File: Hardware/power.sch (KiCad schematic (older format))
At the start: 82 parts, among them J2 USB_B_Micro, J3 B2B-XH-A, J4 POWER ON, Q2 FDC638P, Q3 IRLML6244TRPBF, Q4 BSS138, Q5 BSS138, Q6 IRLML6244TRPBF, Q7 FDC638P, U10 TPS63900DSKR, U11 SiP32431DR3, U12 SiP32431DR3, U8 TP4056, U9 USBLC6-2SC6

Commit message: Add pcb route and ground plane
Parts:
- removed C25: 1u, Capacitor_SMD:C_0603_1608Metric, symbol Device:C
- removed D3, D4, D5, D6: 1N4148, Diode_THT:D_DO-35_SOD27_P7.62mm_Horizontal, symbol Diode:1N4148
- removed DFE252012P-2R2M=P2__2.2µH1: 2.2uH, symbol Device:L
- removed J2: USB_B_Micro, Connector_USB:USB_Micro-B_Wuerth_614105150721_Vertical, symbol Connector:USB_B_Micro
- removed Q4, Q5: BSS138, Package_TO_SOT_SMD:SOT-23, symbol Transistor_FET:BSS138
- removed R58, R59: 0R, Resistor_SMD:R_0603_1608Metric, symbol Device:R
- removed TP19, TP22, TP23, TP24, TP25, TP27, TP29, TP30: TestPoint, TestPoint:TestPoint_Pad_D1.5mm, symbol Connector:TestPoint
- removed U11, U12: SiP32431DR3, Package_TO_SOT_SMD:SOT-363_SC-70-6, symbol Power_Management:SiP32431DR3
- removed U9: USBLC6-2SC6, Package_TO_SOT_SMD:SOT-23-6, symbol Power_Protection:USBLC6-2SC6
- added C44: 0.1u, Capacitor_SMD:C_0603_1608Metric, symbol Device:C
- added D3, D4, D5: 1N4148WT, EcoApi_pcb:SODFL1608X70N, symbol EcoApi_pcb:1N4148WT
- added D8: USBLC6-2SC6, EcoApi_pcb:SOT95P280X145-6N, symbol EcoApi_pcb:USBLC6-2SC6
- added IC2, IC3: SIP32431DR3-T1GE3, EcoApi_pcb:SOT65P210X110-6N, symbol EcoApi_pcb:SIP32431DR3-T1GE3
- added J2: 614105150721, EcoApi_pcb:WURTH_614105150721, symbol EcoApi_pcb:614105150721
- added L2: DFE252012P-2R2M=P2, EcoApi_pcb:INDC2520X120N, symbol EcoApi_pcb:DFE252012P-2R2M=P2
- added Q4, Q5: BSS138, EcoApi_pcb:SOT95P240X111-3N, symbol EcoApi_pcb:BSS138
- added R12, R13: 0R, Resistor_SMD:R_0603_1608Metric, symbol Device:R
- C28: value 0.1u -> 1u
- D1: value LED_0805 -> LED_0603_RED; footprint (none) -> LED_SMD:LED_0603_1608Metric
- D2: value LED_0805 -> LED_0603_GREEN; footprint (none) -> LED_SMD:LED_0603_1608Metric
- D6: renamed from D?; footprint SODFL1608X70N -> EcoApi_pcb:SODFL1608X70N
- TP20, TP21, TP26, TP28: footprint TestPoint:TestPoint_Pad_D1.5mm -> TestPoint:TestPoint_Pad_D1.0mm
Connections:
- wire segments 256 -> 253
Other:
- moved on the sheet: C16, C17, C19, C20, C21, C22, D1, D2, D6, F1, FB1, FB2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

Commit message: Fix drc error
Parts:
- F1, F2: footprint EcoApi_pcb:0603-F1608X100N -> EcoApi_pcb:FUSC1608X100N
- U10: footprint EcoApi_pcb:TPS63900DSKR -> EcoApi_pcb:SON50P250X250X80-11N-D
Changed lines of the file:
@@
 F 0 "U10" H 6000 2337 60  0000 C CNN
 F 1 "TPS63900DSKR" H 6000 2231 60  0000 C CNN
-F 2 "EcoApi_pcb:TPS63900DSKR" H 6000 1300 60  0001 C CNN
+F 2 "EcoApi_pcb:SON50P250X250X80-11N-D" H 6000 1300 60  0001 C CNN
 F 3 "" H 6000 1600 60  0001 C CNN
 	1    6000 1850
@@
 F 0 "F1" V 1165 5850 50  0000 C CNN
 F 1 "MF-FSMF050X-2" V 1256 5850 50  0000 C CNN
-F 2 "EcoApi_pcb:0603-F1608X100N" H 1400 5850 50  0001 L BNN
+F 2 "EcoApi_pcb:FUSC1608X100N" H 1400 5850 50  0001 L BNN
 F 3 "" H 1400 5850 50  0001 L BNN
 F 4 "MF-FSMF050X-2" H 1400 5850 50  0001 L BNN "MPN"
@@
 F 0 "F2" V 2465 1750 50  0000 C CNN
 F 1 "MF-FSMF050X-2" V 2556 1750 50  0000 C CNN
-F 2 "EcoApi_pcb:0603-F1608X100N" H 2700 1750 50  0001 L BNN
+F 2 "EcoApi_pcb:FUSC1608X100N" H 2700 1750 50  0001 L BNN
 F 3 "" H 2700 1750 50  0001 L BNN
 F 4 "MF-FSMF050X-2" H 2700 1750 50  0001 L BNN "MPN"

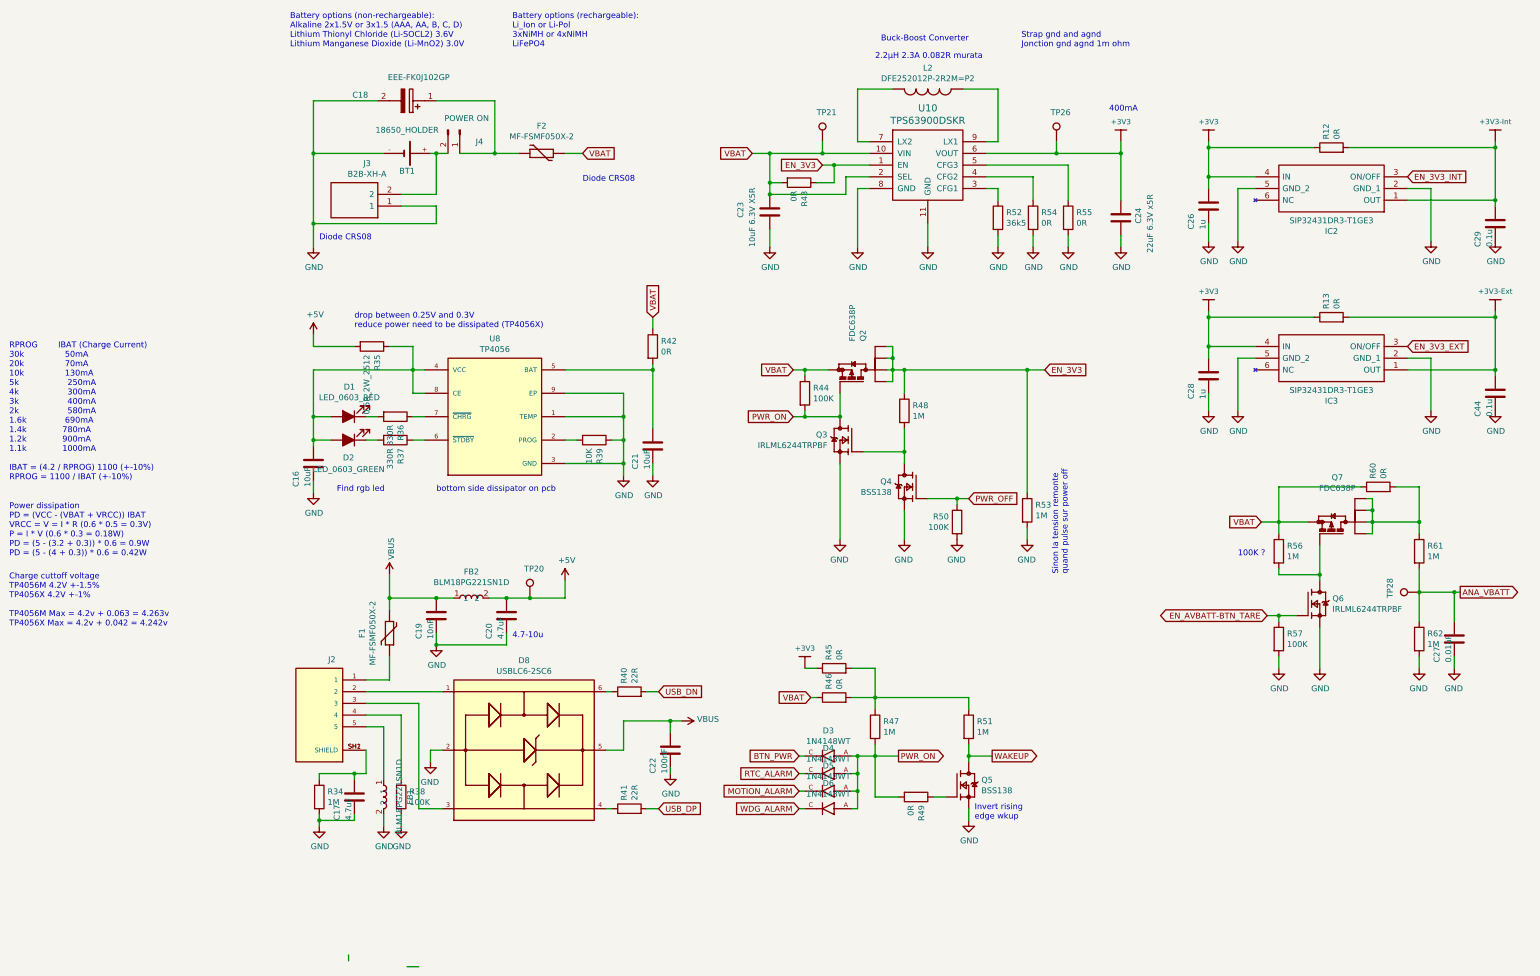
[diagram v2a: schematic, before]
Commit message: Update pcb to v2.1 (Add ldo)
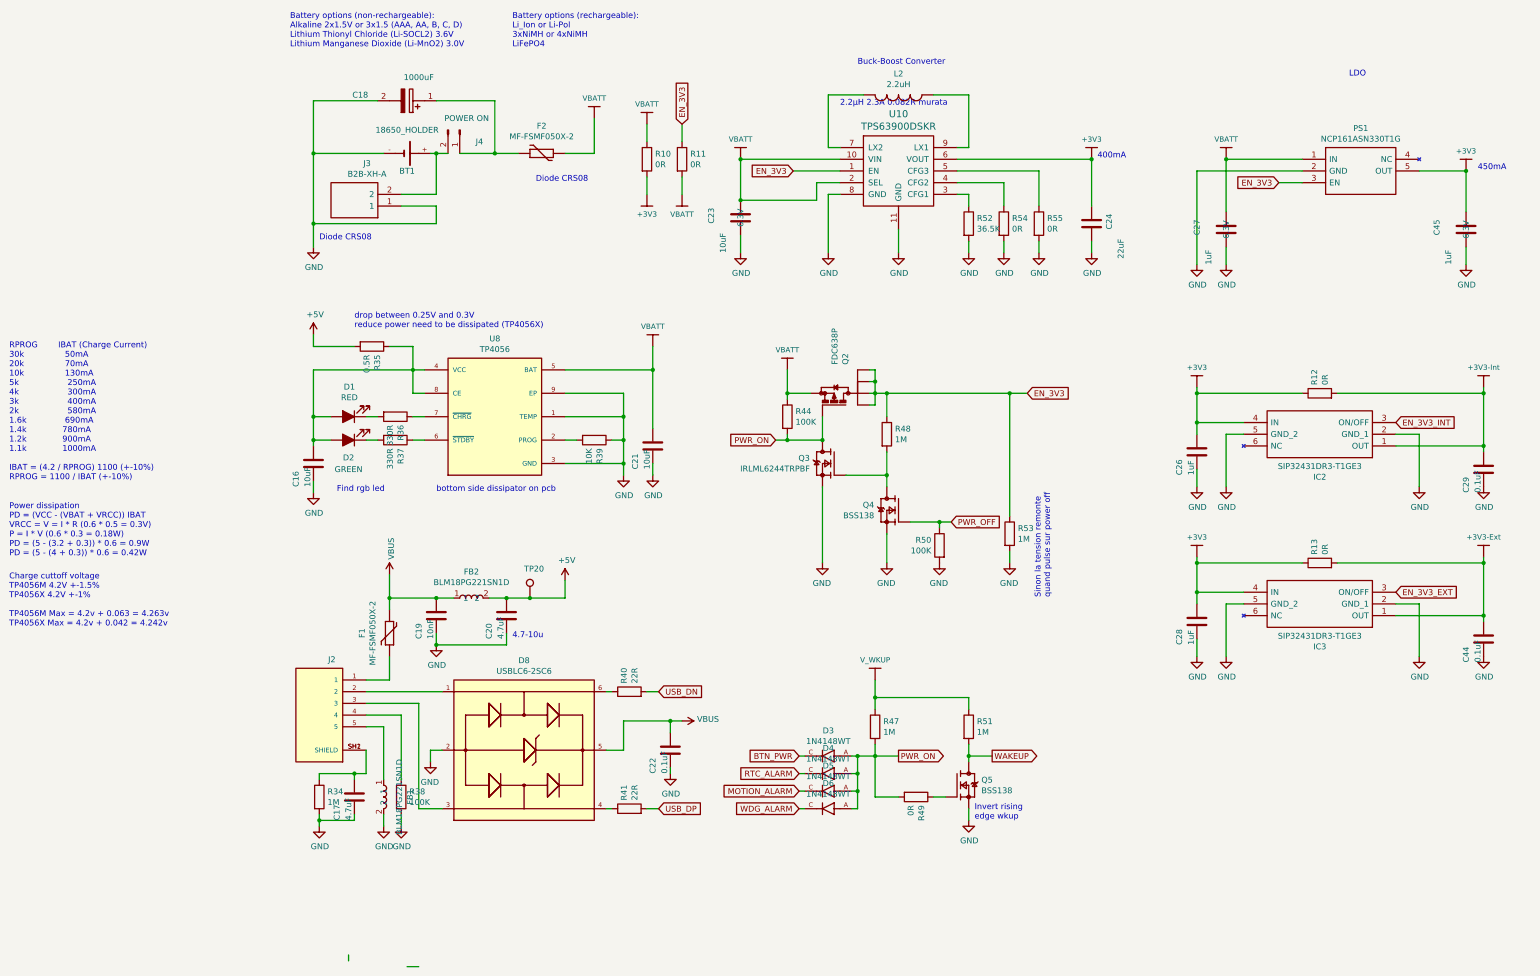
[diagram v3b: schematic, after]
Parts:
- removed Q6: IRLML6244TRPBF, EcoApi_pcb:SOT95P237X112-3N, symbol EcoApi_pcb:IRLML6244TRPBF
- removed Q7: FDC638P, EcoApi_pcb:SSOT-6, symbol EcoApi_pcb:FDC638P
- removed R42, R43, R45, R46, R60: 0R, Resistor_SMD:R_0603_1608Metric, symbol Device:R
- removed R56, R61, R62: 1M, Resistor_SMD:R_0603_1608Metric, symbol Device:R
- removed R57: 100K, Resistor_SMD:R_0603_1608Metric, symbol Device:R
- removed TP21, TP26, TP28: TestPoint, TestPoint:TestPoint_Pad_D1.0mm, symbol Connector:TestPoint
- added C45: 1uF, Capacitor_SMD:C_0603_1608Metric, symbol Device:C
- added PS1: NCP161ASN330T1G, EcoApi_pcb:SOT95P280X145-5N, symbol EcoApi_pcb:NCP161ASN330T1G
- added R10: 0R, Resistor_SMD:R_1206_3216Metric, symbol Device:R
- added R11: 0R, Resistor_SMD:R_0603_1608Metric, symbol Device:R
- BT1, J2, J3, J4: Populate (none) -> no
- C16, C17, C19, C20, C21, FB1, FB2: Populate (none) -> yes; Size Inch (none) -> 0603; Size Metric (none) -> 1608
- C18: value EEE-FK0J102GP -> 1000uF; Manufacturer_Name (none) -> Panasonic; Manufacturer_Part_Number (none) -> EEE-FK0J102GP; Populate (none) -> no; Tolerance (none) -> 20%; Voltage (none) -> 6.3V
- C22: value 100nF -> 0.1uF; Populate (none) -> yes; Size Inch (none) -> 0603; Size Metric (none) -> 1608
- C23: value 10uF 6.3V X5R -> 10uF; Dielectric (none) -> X5R; Populate (none) -> yes; Size Inch (none) -> 0603; Size Metric (none) -> 1608; Voltage (none) -> 6.3V
- C24: value 22uF 6.3V x5R -> 22uF; Dielectric (none) -> X5R; Populate (none) -> yes; Size Inch (none) -> 0603; Size Metric (none) -> 1608; Voltage (none) -> 6.3V
- C26, C28: value 1u -> 1uF; Populate (none) -> yes; Size Inch (none) -> 0603; Size Metric (none) -> 1608
- C27: value 0.01uF -> 1uF; Dielectric (none) -> X5R; Populate (none) -> yes; Size Inch (none) -> 0603; Size Metric (none) -> 1608; Voltage (none) -> 6.3V
- C29, C44: value 0.1u -> 0.1uF; Populate (none) -> yes; Size Inch (none) -> 0603; Size Metric (none) -> 1608
- D1: value LED_0603_RED -> RED; Populate (none) -> yes; Size Inch (none) -> 0603; Size Metric (none) -> 1608
- D2: value LED_0603_GREEN -> GREEN; Populate (none) -> yes; Size Inch (none) -> 0603; Size Metric (none) -> 1608
- D3, D4, D5, D6, F1, F2, TP20: Populate (none) -> yes
- D8: Populate (none) -> yes; package (none) -> SOT-23-6
- IC2, IC3: Populate (none) -> yes; package (none) -> SC-70-6
- L2: value DFE252012P-2R2M=P2 -> 2.2uH; Manufacturer_Name (none) -> Murata Electronics; Manufacturer_Part_Number (none) -> DFE252012P-2R2M=P2; Populate (none) -> yes; Size Inch (none) -> 1008; Size Metric (none) -> 2520; Tolerance (none) -> 20%
- Q2: Manufacturer_Part_Number (none) -> FDC638P; Populate (none) -> yes; package (none) -> SSOT-6
- Q3: Manufacturer_Name (none) -> Infineon; Manufacturer_Part_Number (none) -> IRLML6244TRPBF; Populate (none) -> yes; package (none) -> SOT-23-3
- Q4, Q5: Manufacturer_Name (none) -> onsemi; Manufacturer_Part_Number (none) -> BSS138; Populate (none) -> yes; package (none) -> SOT-23-3
- R12, R13: Populate (none) -> no; Size Inch (none) -> 0603; Size Metric (none) -> 1608; Tolerance (none) -> 1%
- R34, R36, R37, R38, R39, R40, R41, R44, R47, R48, R49, R50, R51, R53, R54, R55: Populate (none) -> yes; Size Inch (none) -> 0603; Size Metric (none) -> 1608; Tolerance (none) -> 1%
- R35: value 0.5R_2W_2512 -> 0.5R; footprint Resistor_SMD:R_0603_1608Metric -> Resistor_SMD:R_2512_6332Metric; Populate (none) -> yes; Power Rating (none) -> 2W; Size Inch (none) -> 6332; Size Metric (none) -> 2512; Tolerance (none) -> 1%
- R52: value 36k5 -> 36.5K; Populate (none) -> yes; Size Inch (none) -> 0603; Size Metric (none) -> 1608; Tolerance (none) -> 1%
- U10: Manufacturer_Name (none) -> Texas Instruments; Manufacturer_Part_Number (none) -> TPS63900DSKR; Populate (none) -> no; package (none) -> WSON-10
- U8: Manufacturer_Name (none) -> TPower; Manufacturer_Part_Number (none) -> TP4056; Populate (none) -> yes; package (none) -> SOP-8
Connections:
- net ANA_VBATT is gone; now on net VBATT: C27.1
- net VBAT is gone; now on net VBATT: C23.1, F2.2, Q2.4, R44.1, U10.10 (VIN), U10.2 (SEL)
- net +3V3: now also C45.1, PS1.5 (OUT), R10.2
- net EN_3V3: now also PS1.3 (EN), R11.1
- net GND: now also C45.2, PS1.2 (GND)
- net VBATT: now reaches C21.1, U8.5 (BAT)
- net VBATT: now also PS1.1 (IN), R10.1, R11.2
- net V_WKUP: now reaches R47.1, R51.1
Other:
- note added: "450mA"
- note added: "LDO"
- note removed: "100K ?"
- note removed: "Strap gnd and agnd\nJonction gnd agnd 1m ohm"
- moved on the sheet: C23, C24, C26, C28, C29, C44, IC2, IC3, L2, Q2, Q3, Q4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
